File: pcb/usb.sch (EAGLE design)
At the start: 46 parts, among them CN2 JSTPH, CN3 AMP FCI 10103594-0001LF, Q1 mmbt2222, Q2 mmbt2222, U1 UG-2828GDEDF11, U2 MIC5225-3.3v, U3 FAN5331SX, U4 CH340G, U6 MCP73831T-2ACI/OT, Y2 12MHz

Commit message: Board updates
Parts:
- removed C1, C2: 10uF/16V, microbuilder:CAP_CERAMIC0805
- removed C10: 10uF, adafruit:C-USC0805
- removed C3, C4: 1.0uF, microbuilder:CAP_CERAMIC0805
- removed C5, C7: 10uF, microbuilder:CAP_CERAMIC0805
- removed C8: 0.1uF, microbuilder:CAP_CERAMIC0805
- removed CN3: AMP FCI 10103594-0001LF, SparkFun-Connectors:USB_MICRO-B_HALF_PTH
- removed D1, D3: 1N4148, microbuilder:DIODESOD-323
- removed D2: BAT54T1G, microbuilder:DIODESOD-123
- removed L1: 10uH, microbuilder:INDUCTOR
- removed R10, R11, R12, R13: 10K, adafruit:R-US_R0805
- removed R4: 600K, microbuilder:RESISTOR0805
- removed R5: 50, microbuilder:RESISTOR0805
- removed R6: 100K, microbuilder:RESISTOR0805
- removed R7, R8: 10K, microbuilder:RESISTOR0805
- removed S1: (no value), SparkFun-Switches:SWITCH-SPDT-SMD-RIGHT-ANGLE
- removed U1: UG-2828GDEDF11, microbuilder:DISP_OLED_UG-2828GDEDF11TOP
- removed U3: FAN5331SX, microbuilder:FAN5331
- removed X1: (no value), adafruit:ESP-12
- added J1: (no value), Wurth_Elektronik_Electromechanic_Input-Output_Connectors_rev19a:614105150621
- added JP1, JP2: (no value), adafruit:PINHD-1X8CLEANBIG
- added JP3: JUMPER-SMT_2_NC_TRACE_NO-SILK, SparkFun-Jumpers:JUMPER-SMT_2_NC_TRACE_NO-SILK
- U6: device microbuilder:MCP73831/2 -> adafruit:MCP73831/OT
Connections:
- removed net 13V: C1.P$2, C8.P$1, D2.C, R6.2, U1.VCC
- removed net 3.3V: C3.P$2, C5.P$1, C7.P$1, L1.1, U1.VCI, U1.VDDIO, U2.OUT, U3.SHDN, U3.VIN
- removed net CH_PD: R10.2, X1.CH_PD
- removed net IREF: R4.2, U1.IREF
- removed net MOSI/DATA1: U1.D1/SDIN, X1.GPIO13
- removed net N$11: D1.C, D3.A
- removed net N$17: R13.1, X1.GPIO15
- removed net N$3: C4.P$1, U1.VDD
- removed net N$5: D2.A, L1.2, U3.SW
- removed net N$6: R5.2, U1.VSL
- removed net N$7: D1.A, R5.1
- removed net N$8: C8.P$2, R6.1, R7.2, U3.FB
- removed net OLED_BS0: R8.2, U1.BS0
- removed net OLED_CS: U1.CS#, X1.GPIO16
- removed net OLED_DC: U1.D/C#, X1.GPIO4
- removed net OLED_RES: U1.RES#, X1.GPIO5
- removed net SCK/DATA0: U1.D0/SCK, X1.GPIO14
- removed net VCOMH: C2.P$1, U1.VCOMH
- new net +3.3V: U2.OUT
- new net 5V: JP2.8
- new net A0: JP1.7
- new net D0/GPIO16: JP1.6
- new net D1/GPIO5: JP2.3
- new net D2/GPIO4: JP2.4
- new net D3/GPIO0: JP2.5
- new net D4/GPIO2: JP2.6
- new net D5/GPIO14/SCK: JP1.5
- new net D6/GPIO12: JP1.4
- new net D7/GPIO13/MOSI: JP1.3
- new net D8/GPIO15: JP1.2
- net +3V3: now also JP1.1; no longer C10.1, R10.1, R11.1, R12.2, X1.VCC
- net D+: now also J1.D+; no longer CN3.D+
- net D-: now also J1.D-; no longer CN3.D-
- net GND: now also J1.GND, JP2.7; no longer C1.P$1, C10.2, C2.P$2, C3.P$1, C4.P$2, C5.P$2, C7.P$2, CN3.GND, CN3.SHIELD, D3.C, R13.2, R4.1, R7.1, R8.1, U1.BS1, U1.NC(GND)@1, U1.NC(GND)@2, U1.VSS, U3.GND, X1.GND
- net GPIO0: no longer R12.1, X1.GPIO0
- net N$19: now also JP3.1; no longer S1.P
- net RESET: now also JP1.8; no longer R11.2, X1.RESET
- net RX: now also JP2.2; no longer X1.RXD
- net TX: now also JP2.1; no longer X1.TXD
- net VBAT: now also JP3.2; no longer S1.S
- net VBUS: now also J1.VBUS; no longer CN3.VBUS
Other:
- note removed: "13V Boost"
- note removed: "= (13.5-6)/.0000125"
- note removed: "= 600K"
- note removed: "D1+D3 must be >= 1.4V"
- note removed: "R4 = (VCC-6V)/12.5uA"
- note removed: "This is 0.5V above the recommended voltage,"
- note removed: "VDD generated"
- note removed: "VOUT = 1.23V * (1 + R6/R7)"
- note removed: "VOUT = 13.53V"
- note removed: "but uses common resistors for easy assembly"
- note removed: "internally"
- moved on the sheet: C12, C13, C6, CHG, CN2, D5, Q1, Q2, R1, R2, R3, R9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

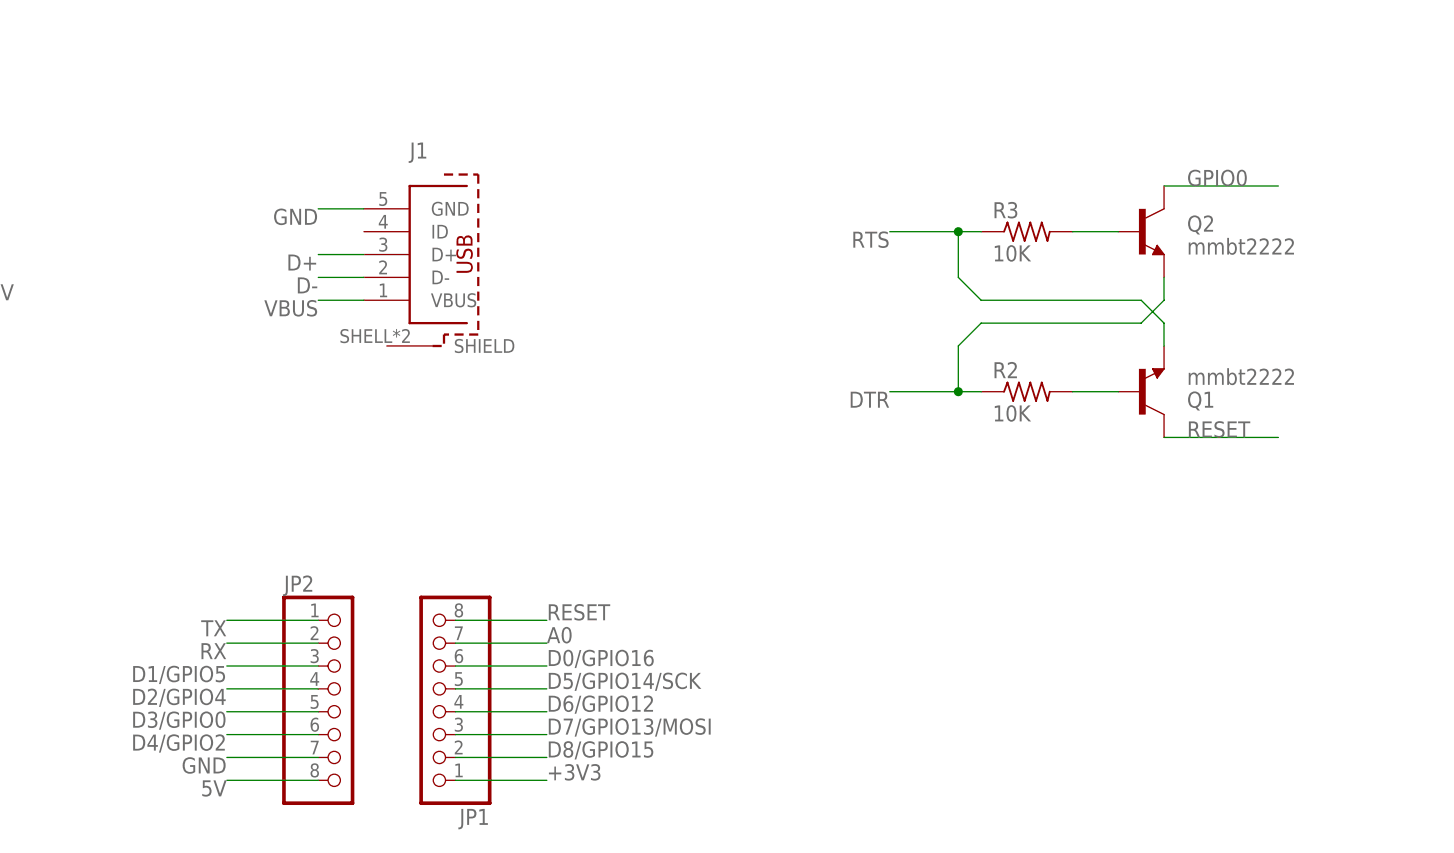
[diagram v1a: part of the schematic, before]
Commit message: Add USB board layout
Committing on master :)
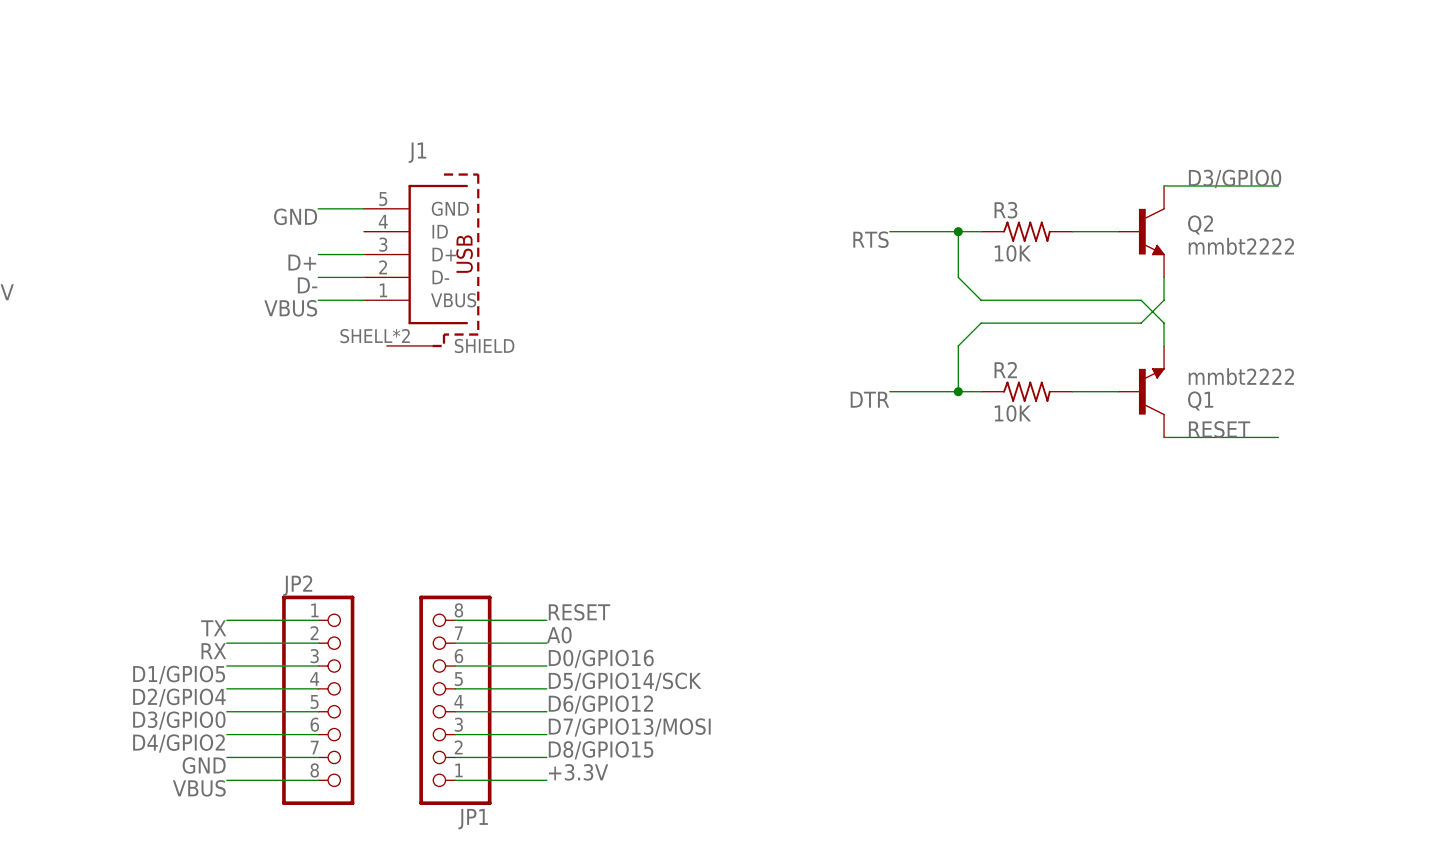
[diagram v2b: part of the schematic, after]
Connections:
- removed net +3V3: JP1.1
- removed net 5V: JP2.8
- removed net GPIO0: Q2.C
- net +3.3V: now also JP1.1
- net D3/GPIO0: now also Q2.C
- net VBUS: now also JP2.8
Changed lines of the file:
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@@
 <label x="88.9" y="86.36" size="1.778" layer="95"/>
+</segment>
+<segment>
+<pinref part="JP1" gate="G$1" pin="1"/>
+<wire x1="144.78" y1="33.02" x2="154.94" y2="33.02" width="0.1524" layer="91"/>
+<label x="154.94" y="33.02" size="1.778" layer="95"/>
 </segment>
 </net>
@@
 <label x="129.54" y="86.36" size="1.778" layer="95" rot="R180"/>
 </segment>
+<segment>
+<pinref part="JP2" gate="G$1" pin="8"/>
+<wire x1="129.54" y1="33.02" x2="119.38" y2="33.02" width="0.1524" layer="91"/>
+<label x="119.38" y="33.02" size="1.778" layer="95" rot="R180"/>
+</segment>
 </net>
 <net name="N$19" class="1">
@@
 <wire x1="144.78" y1="50.8" x2="154.94" y2="50.8" width="0.1524" layer="91"/>
 <label x="154.94" y="50.8" size="1.778" layer="95"/>
-</segment>
-</net>
-<net name="GPIO0" class="0">
-<segment>
-<wire x1="223.52" y1="99.06" x2="236.22" y2="99.06" width="0.1524" layer="91"/>
-<label x="226.06" y="99.06" size="1.778" layer="95"/>
-<pinref part="Q2" gate="G$1" pin="C"/>
 </segment>
 </net>
@@
 </segment>
 </net>
-<net name="+3V3" class="1">
-<segment>
-<pinref part="JP1" gate="G$1" pin="1"/>
-<wire x1="144.78" y1="33.02" x2="154.94" y2="33.02" width="0.1524" layer="91"/>
-<label x="154.94" y="33.02" size="1.778" layer="95"/>
-</segment>
-</net>
 <net name="D1/GPIO5" class="0">
 <segment>
@@
 <label x="119.38" y="40.64" size="1.778" layer="95" rot="R180"/>
 </segment>
+<segment>
+<wire x1="223.52" y1="99.06" x2="236.22" y2="99.06" width="0.1524" layer="91"/>
+<label x="226.06" y="99.06" size="1.778" layer="95"/>
+<pinref part="Q2" gate="G$1" pin="C"/>
+</segment>
 </net>
 <net name="D4/GPIO2" class="0">
@@
 </segment>
 </net>
-<net name="5V" class="0">
-<segment>
-<pinref part="JP2" gate="G$1" pin="8"/>
-<wire x1="129.54" y1="33.02" x2="119.38" y2="33.02" width="0.1524" layer="91"/>
-<label x="119.38" y="33.02" size="1.778" layer="95" rot="R180"/>
-</segment>
-</net>

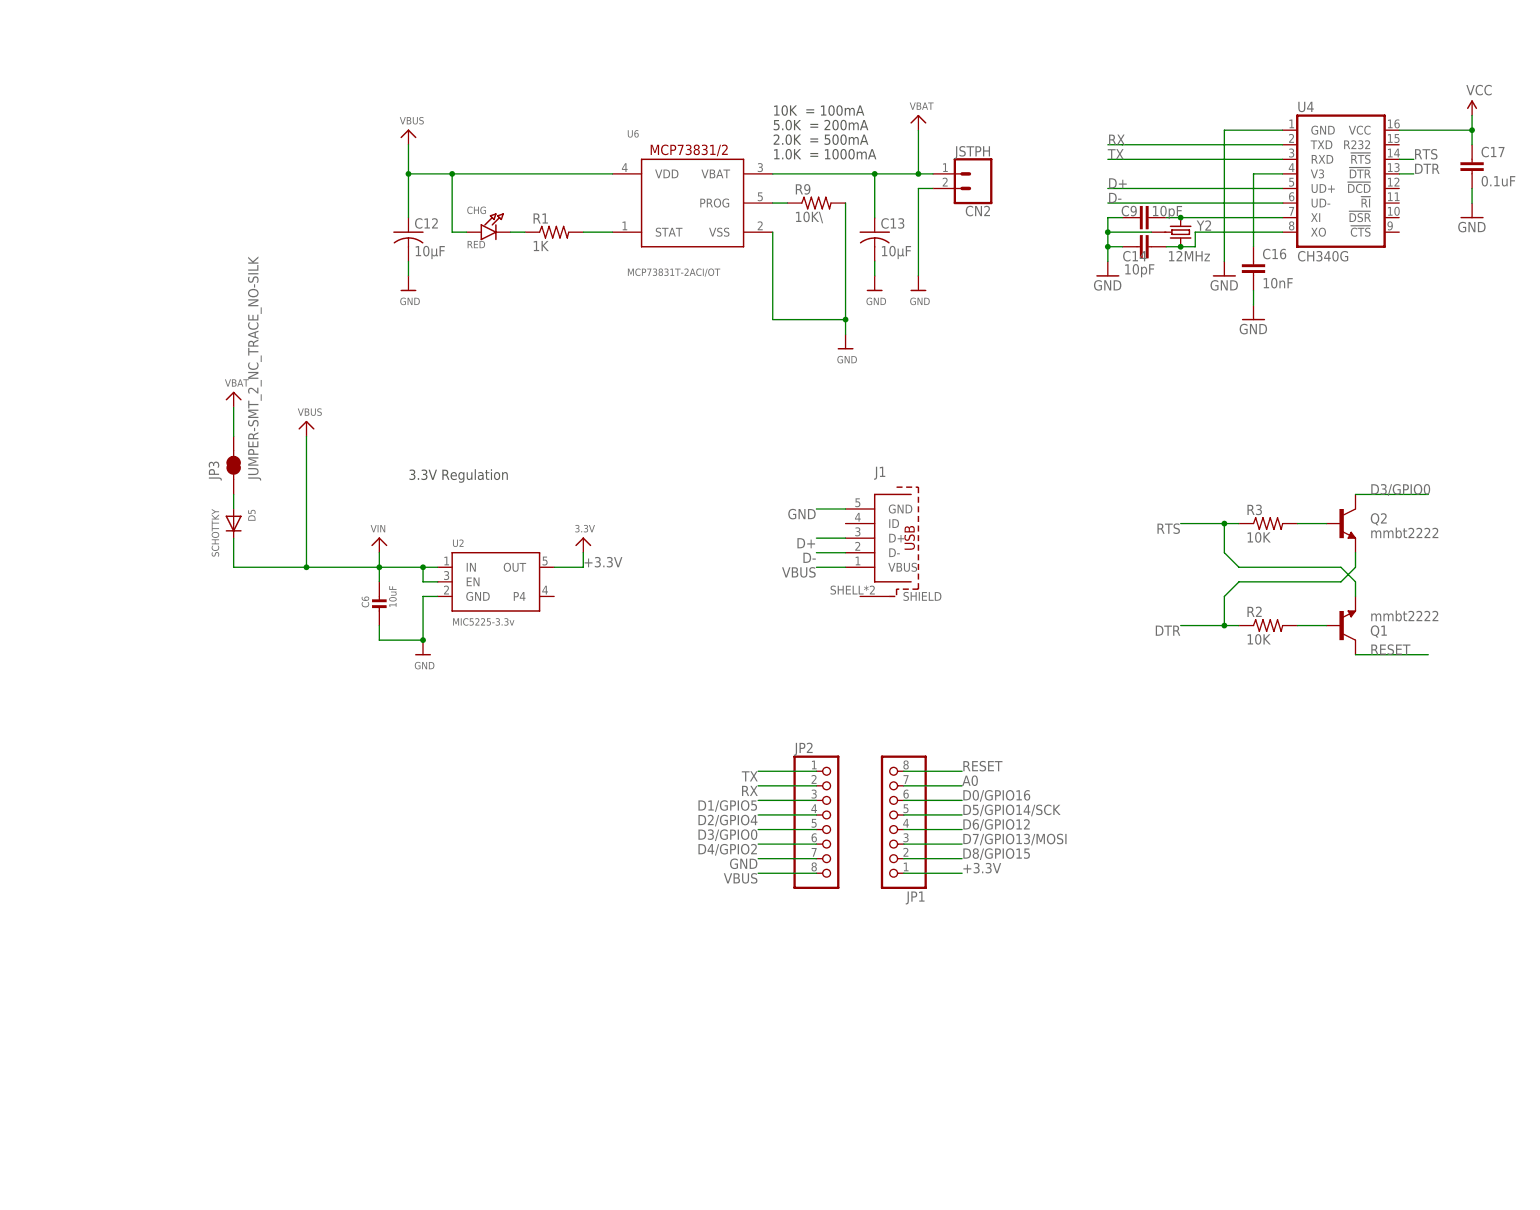
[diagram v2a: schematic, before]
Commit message: USB board schematic V2 done
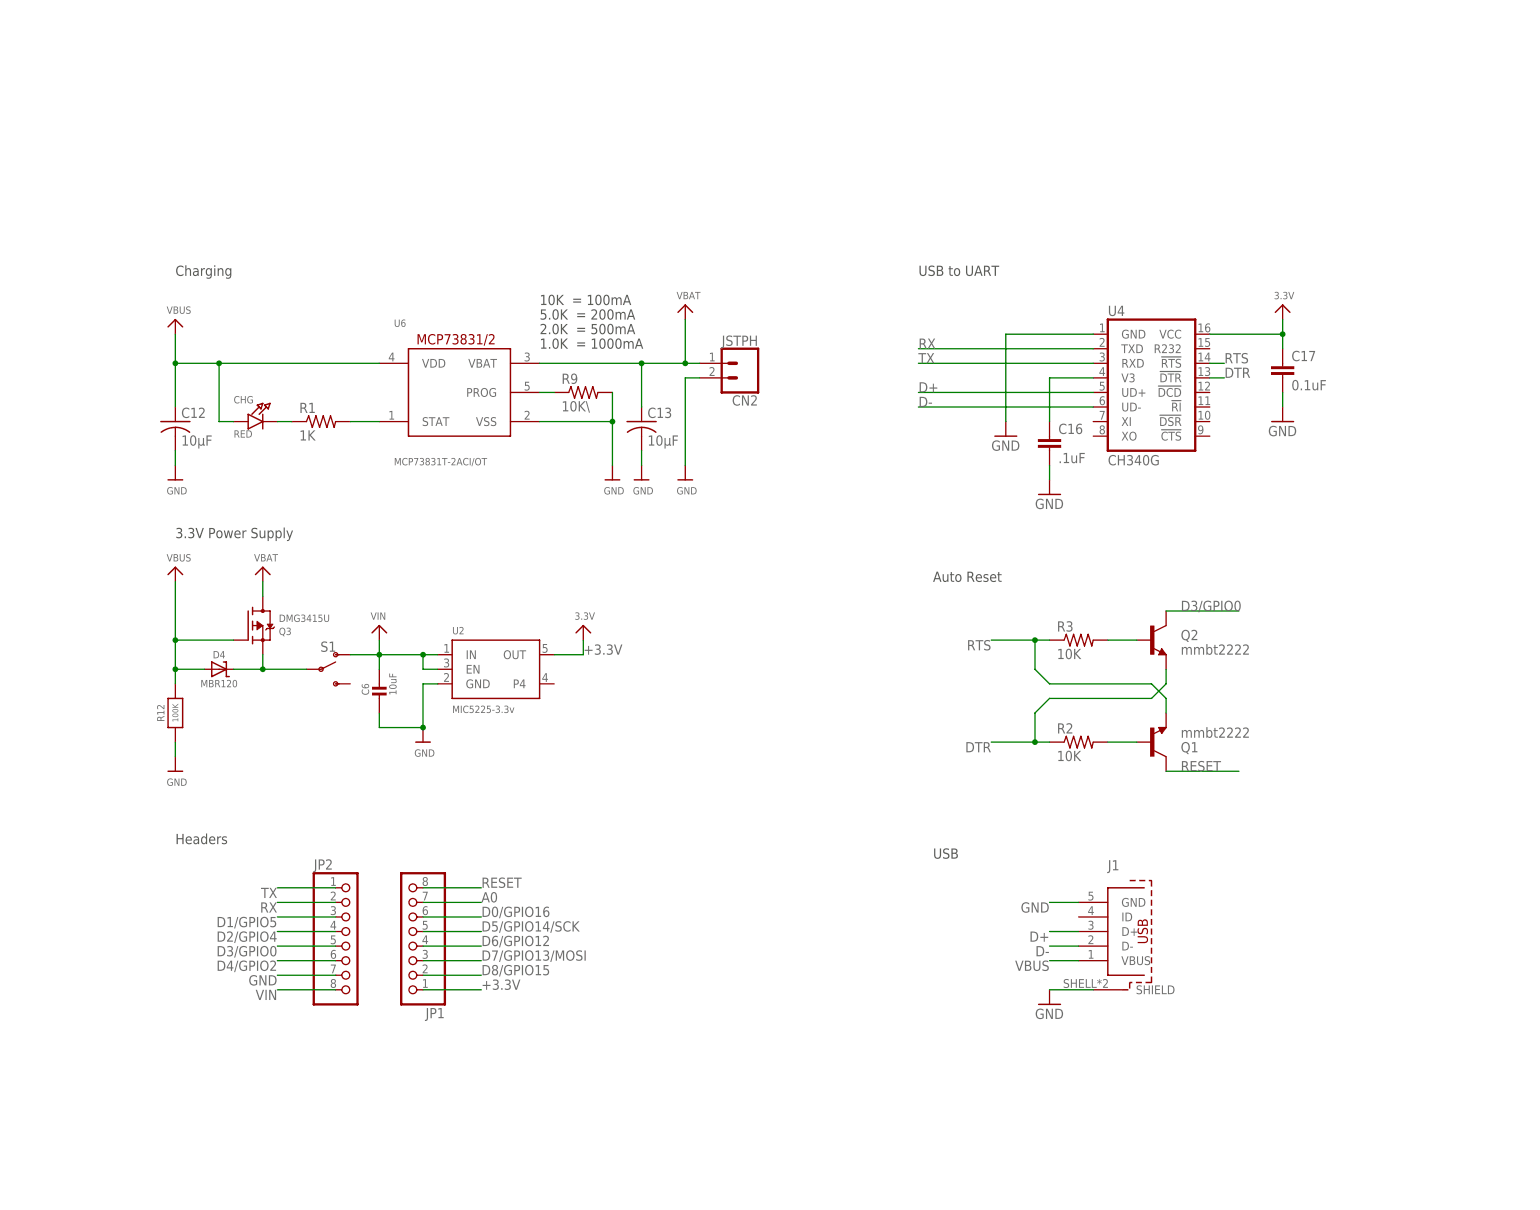
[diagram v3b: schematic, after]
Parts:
- removed C14, C9: 10pF, SparkFun-Capacitors:10PF-50V-5%(0603)
- removed D5: SCHOTTKY, adafruit:DIODE_SOD-123FL
- removed JP3: JUMPER-SMT_2_NC_TRACE_NO-SILK, SparkFun-Jumpers:JUMPER-SMT_2_NC_TRACE_NO-SILK
- removed Y2: 12MHz, USB Basic:CRYSTAL-GROUNDED3.2X2.5
- added D4: MBR120, microbuilder:DIODE-SCHOTTKYSOD-123
- added Q3: DMG3415U, microbuilder:MOSFET-P
- added R12: 100K, microbuilder:RESISTOR_0603_NOOUT
- added S1: (no value), SparkFun-Switches:SWITCH-SPDT-SMD-AYZ0202
- C16: value 10nF -> .1uF
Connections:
- net VCC renamed 3.3V
- removed net N$10: C14.2, U4.XO, Y2.2
- removed net N$12: C9.2, U4.XI, Y2.1
- removed net N$19: D5.A, JP3.1
- new net N$7: D4.C, Q3.S, S1.P
- new net VIN: C6.P$1, JP2.8, S1.O, U2.EN, U2.IN
- net GND: now also J1.SHIELD, R12.1; no longer C14.1, C9.1, Y2.GND
- net VBAT: now also Q3.D; no longer JP3.2
- net VBUS: now also D4.A, Q3.G, R12.2; no longer C6.P$1, D5.C, JP2.8, U2.EN, U2.IN
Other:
- note added: "3.3V Power Supply"
- note added: "Auto Reset"
- note added: "Charging"
- note added: "Headers"
- note added: "USB"
- note added: "USB to UART"
- note removed: "3.3V Regulation"
- moved on the sheet: C12, C13, C16, C17, C6, CHG, CN2, J1, JP1, JP2, Q1, Q2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
